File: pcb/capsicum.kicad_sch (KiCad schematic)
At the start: 45 parts, among them J1 USB4510-03-1-A_REVA, J2 Screw_Terminal_01x02, Q1 PN2222A, SW1 SW_SPDT, SW2 SW_Push_Dual, SW3 SW_SPDT, SW4 SW_Push_Dual, U1 ESP32-C3-WROOM-02, U3 AP2112K-3.3, U4 MCP73831-2-OT

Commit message: feat: associate 0603 capcitors and resistors footprints
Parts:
- C1, C2, C3, C4, C5, C6, C7, C8: footprint (none) -> Capacitor_SMD:C_0603_1608Metric
- D1, D2, D3, D4, D5, R1, R10, R11, R12, R13, R2, R3, R4, R5, R6, R7, R8, R9: footprint (none) -> Resistor_SMD:R_0603_1608Metric
- J1: footprint USB4510-03-1-A_REVA:GCT_USB4510-03-1-A_REVA -> GCT_USB_C:GCT_USB4510-03-1-A_REVA
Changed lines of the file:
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@@
       (effects (font (size 1.27 1.27)) (justify left))
     )
-    (property "Footprint" "" (at 218.44 68.58 0)
+    (property "Footprint" "Resistor_SMD:R_0603_1608Metric" (at 218.44 68.58 0)
       (effects (font (size 1.27 1.27)) hide)
     )
@@
       (effects (font (size 1.27 1.27)) (justify right))
     )
-    (property "Footprint" "" (at 218.44 62.23 0)
+    (property "Footprint" "Resistor_SMD:R_0603_1608Metric" (at 218.44 62.23 0)
       (effects (font (size 1.27 1.27)) hide)
     )
@@
       (effects (font (size 1.27 1.27)))
     )
-    (property "Footprint" "" (at 250.19 27.94 0)
+    (property "Footprint" "Resistor_SMD:R_0603_1608Metric" (at 250.19 27.94 0)
       (effects (font (size 1.27 1.27)) hide)
     )
@@
       (effects (font (size 1.27 1.27)))
     )
-    (property "Footprint" "" (at 120.65 64.77 0)
+    (property "Footprint" "Resistor_SMD:R_0603_1608Metric" (at 120.65 64.77 0)
       (effects (font (size 1.27 1.27)) hide)
     )
@@
       (effects (font (size 1.27 1.27)) (justify right))
     )
-    (property "Footprint" "" (at 196.85 73.66 0)
+    (property "Footprint" "Resistor_SMD:R_0603_1608Metric" (at 196.85 73.66 0)
       (effects (font (size 1.27 1.27)) hide)
     )
@@
       (effects (font (size 1.27 1.27)) (justify left))
     )
-    (property "Footprint" "" (at 186.69 64.77 0)
+    (property "Footprint" "Resistor_SMD:R_0603_1608Metric" (at 186.69 64.77 0)
       (effects (font (size 1.27 1.27)) hide)
     )
@@
       (effects (font (size 1.27 1.27)) (justify left))
     )
-    (property "Footprint" "" (at 20.32 48.26 0)
+    (property "Footprint" "Resistor_SMD:R_0603_1608Metric" (at 20.32 48.26 0)
       (effects (font (size 1.27 1.27)) hide)
     )
@@
       (effects (font (size 1.27 1.27)) (justify left))
     )
-    (property "Footprint" "" (at 259.08 66.04 0)
+    (property "Footprint" "Resistor_SMD:R_0603_1608Metric" (at 259.08 66.04 0)
       (effects (font (size 1.27 1.27)) hide)
     )
@@
       (effects (font (size 1.27 1.27)))
     )
-    (property "Footprint" "" (at 182.88 38.1 0)
+    (property "Footprint" "Resistor_SMD:R_0603_1608Metric" (at 182.88 38.1 0)
       (effects (font (size 1.27 1.27)) hide)
     )
@@
       (effects (font (size 1.27 1.27)) (justify left))
     )
-    (property "Footprint" "" (at 153.3652 72.39 0)
+    (property "Footprint" "Capacitor_SMD:C_0603_1608Metric" (at 153.3652 72.39 0)
       (effects (font (size 1.27 1.27)) hide)
     )
@@
       (effects (font (size 1.27 1.27)) (justify left))
     )
-    (property "Footprint" "" (at 34.29 179.07 0)
+    (property "Footprint" "Capacitor_SMD:C_0603_1608Metric" (at 34.29 179.07 0)
       (effects (font (size 1.27 1.27)) hide)
     )
@@
       (effects (font (size 1.27 1.27)) (justify left))
     )
-    (property "Footprint" "" (at 160.02 161.29 0)
+    (property "Footprint" "Resistor_SMD:R_0603_1608Metric" (at 160.02 161.29 0)
       (effects (font (size 1.27 1.27)) hide)
     )
@@
       (effects (font (size 1.27 1.27)) (justify left))
     )
-    (property "Footprint" "" (at 252.73 73.66 0)
+    (property "Footprint" "Capacitor_SMD:C_0603_1608Metric" (at 252.73 73.66 0)
       (effects (font (size 1.27 1.27)) hide)
     )
@@
       (effects (font (size 1.27 1.27)) (justify left))
     )
-    (property "Footprint" "" (at 220.98 36.83 0)
+    (property "Footprint" "Capacitor_SMD:C_0603_1608Metric" (at 220.98 36.83 0)
       (effects (font (size 1.27 1.27)) hide)
     )
@@
       (effects (font (size 1.27 1.27)))
     )
-    (property "Footprint" "USB4510-03-1-A_REVA:GCT_USB4510-03-1-A_REVA" (at 50.8 48.26 0)
+    (property "Footprint" "GCT_USB_C:GCT_USB4510-03-1-A_REVA" (at 50.8 48.26 0)
       (effects (font (size 1.27 1.27)) (justify bottom) hide)
     )
@@
       (effects (font (size 1.27 1.27)) (justify left))
     )
-    (property "Footprint" "" (at 76.2 55.88 0)
+    (property "Footprint" "Resistor_SMD:R_0603_1608Metric" (at 76.2 55.88 0)
       (effects (font (size 1.27 1.27)) hide)
     )
@@
       (effects (font (size 1.27 1.27)) (justify left))
     )
-    (property "Footprint" "" (at 143.2052 72.39 0)
+    (property "Footprint" "Capacitor_SMD:C_0603_1608Metric" (at 143.2052 72.39 0)
       (effects (font (size 1.27 1.27)) hide)
     )
@@
       (effects (font (size 1.27 1.27)))
     )
-    (property "Footprint" "" (at 105.41 62.23 0)
+    (property "Footprint" "Resistor_SMD:R_0603_1608Metric" (at 105.41 62.23 0)
       (effects (font (size 1.27 1.27)) hide)
     )
@@
       (effects (font (size 1.27 1.27)) (justify left))
     )
-    (property "Footprint" "" (at 189.23 26.67 0)
+    (property "Footprint" "Capacitor_SMD:C_0603_1608Metric" (at 189.23 26.67 0)
       (effects (font (size 1.27 1.27)) hide)
     )
@@
       (effects (font (size 1.27 1.27)) (justify left))
     )
-    (property "Footprint" "" (at 196.85 64.77 0)
+    (property "Footprint" "Resistor_SMD:R_0603_1608Metric" (at 196.85 64.77 0)
       (effects (font (size 1.27 1.27)) hide)
     )
@@
       (effects (font (size 1.27 1.27)) (justify left))
     )
-    (property "Footprint" "" (at 115.2652 76.2 0)
+    (property "Footprint" "Capacitor_SMD:C_0603_1608Metric" (at 115.2652 76.2 0)
       (effects (font (size 1.27 1.27)) hide)
     )
@@
       (effects (font (size 1.27 1.27)))
     )
-    (property "Footprint" "" (at 215.9 26.67 0)
+    (property "Footprint" "Resistor_SMD:R_0603_1608Metric" (at 215.9 26.67 0)
       (effects (font (size 1.27 1.27)) hide)
     )
@@
       (effects (font (size 1.27 1.27)) (justify left))
     )
-    (property "Footprint" "" (at 157.48 115.57 0)
+    (property "Footprint" "Resistor_SMD:R_0603_1608Metric" (at 157.48 115.57 0)
       (effects (font (size 1.27 1.27)) hide)
     )
@@
       (effects (font (size 1.27 1.27)) (justify left))
     )
-    (property "Footprint" "" (at 227.33 36.83 0)
+    (property "Footprint" "Capacitor_SMD:C_0603_1608Metric" (at 227.33 36.83 0)
       (effects (font (size 1.27 1.27)) hide)
     )
@@
       (effects (font (size 1.27 1.27)))
     )
-    (property "Footprint" "" (at 250.19 35.56 0)
+    (property "Footprint" "Resistor_SMD:R_0603_1608Metric" (at 250.19 35.56 0)
       (effects (font (size 1.27 1.27)) hide)
     )
@@
       (effects (font (size 1.27 1.27)) (justify right))
     )
-    (property "Footprint" "" (at 186.69 73.66 0)
+    (property "Footprint" "Resistor_SMD:R_0603_1608Metric" (at 186.69 73.66 0)
       (effects (font (size 1.27 1.27)) hide)
     )
@@
       (effects (font (size 1.27 1.27)))
     )
-    (property "Footprint" "" (at 205.74 22.86 0)
-      (effects (font (size 1.27 1.27)) hide)
-    )
+    (property "Footprint" "Resistor_SMD:R_0603_1608Metric" (at 205.74 22.86 0)
+      (effects (font (size 1.27 1.27)) hide)
+    )

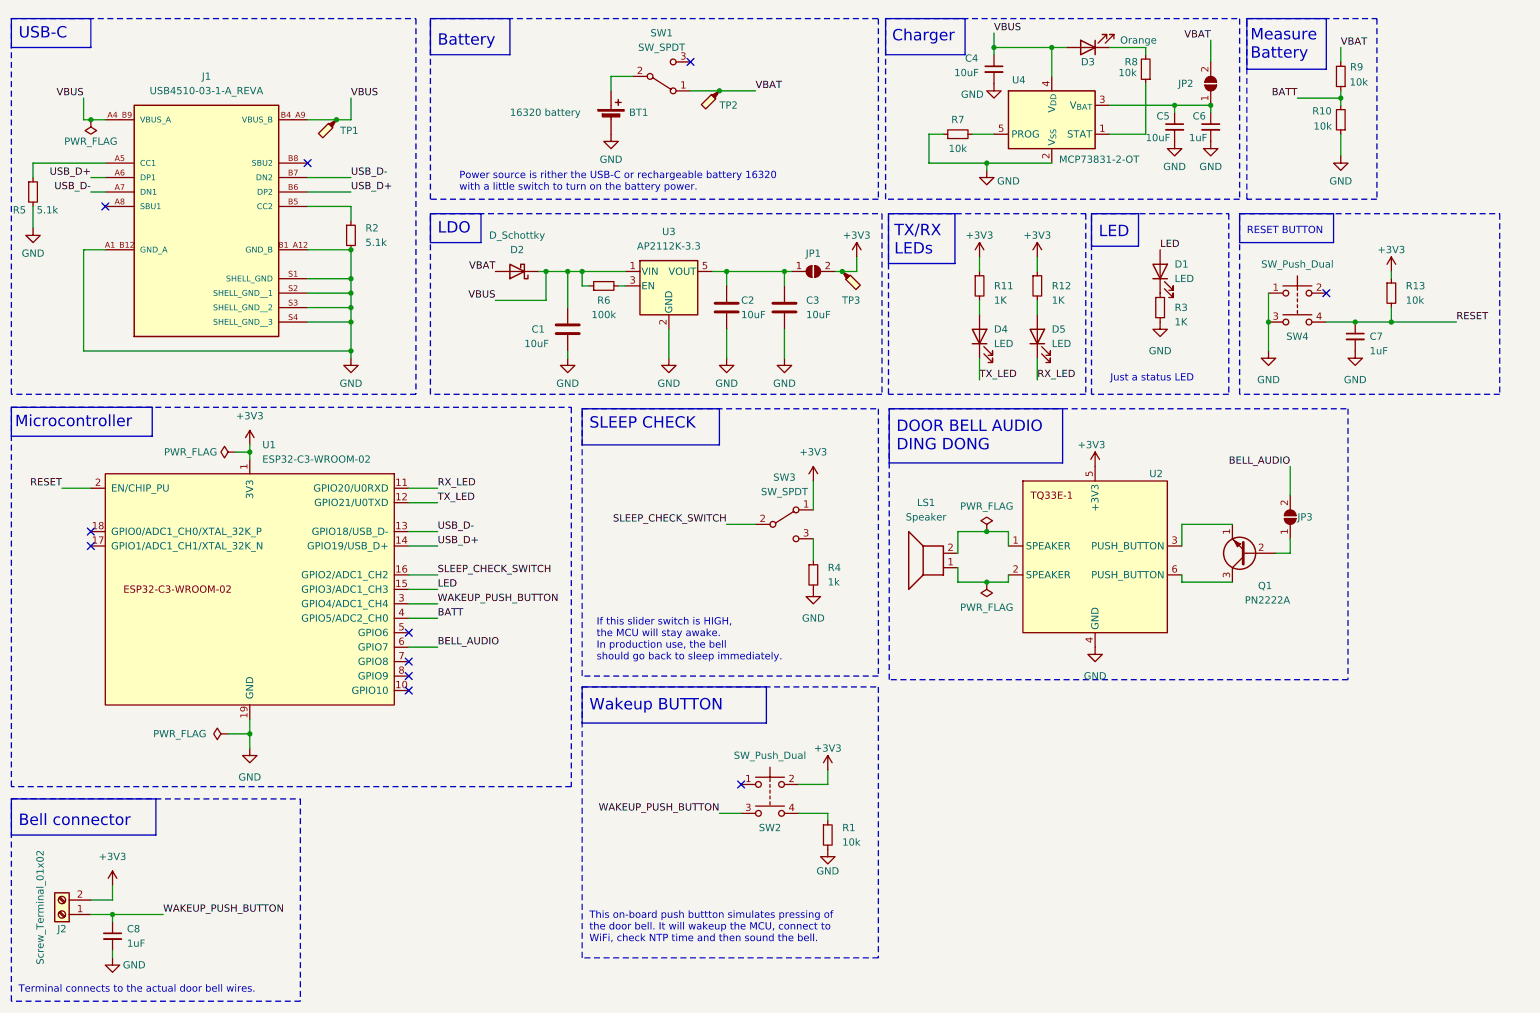
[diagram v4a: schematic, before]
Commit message: refactor: add power LEDs, combine wakeup button schematic and simplify comment
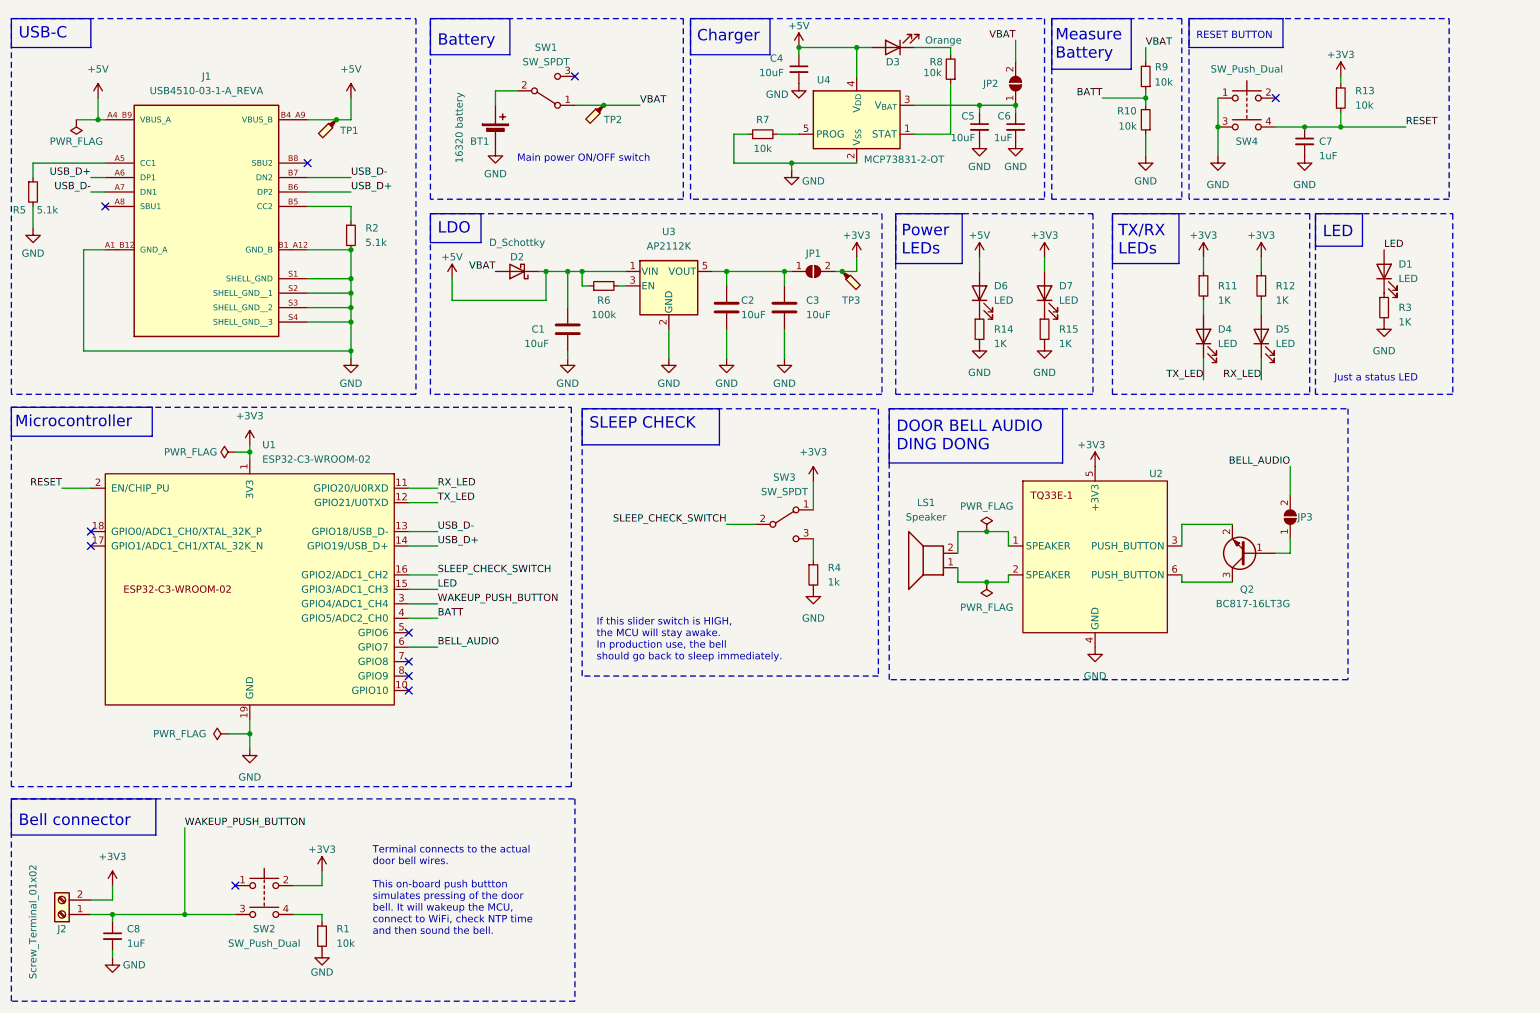
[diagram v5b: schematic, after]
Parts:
- removed Q1: PN2222A, Package_TO_SOT_THT:TO-92_Inline, symbol Transistor_BJT:PN2222A
- added D6, D7: LED, Resistor_SMD:R_0603_1608Metric, symbol Device:LED
- added Q2: BC817-16LT3G, Package_TO_SOT_SMD:SOT-23, symbol Transistor_BJT:BC817
- added R14, R15: 1K, Resistor_SMD:R_0603_1608Metric, symbol Device:R_Small
- C1, C2, C3, C4, C5: Link (none) -> https://www.pcbway.com/components/detail/CC0603KRX5R6BB106/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; MPN (none) -> CC0603KRX5R6BB106; Vendor (none) -> PCBWay
- C6, C7, C8: Link (none) -> https://www.pcbway.com/components/detail/06033D105MAT2A/217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; MPN (none) -> 06033D105MAT2A; Vendor (none) -> PCBWay
- U3: value AP2112K-3.3 -> AP2112K; Link (none) -> https://www.pcbway.com/components/detail/AP2112K33TRG1/1123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; MPN (none) -> AP2112K-3.3TRG1
- U4: MPN (none) -> MCP73831-2-OT
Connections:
- net +3V3: now also D7.2 (A)
- net GND: now also R14.2, R15.2
- net at U2.3 (PUSH_BUTTON): now also Q2.2 (E)
- net at JP3.1 (A): now also Q2.1 (B)
- net at U2.6 (PUSH_BUTTON): now also Q2.3 (C)
- net VBUS renamed +5V
- net +5V: now also D6.2 (A)
- new net: D6.1 (K), R14.1
- new net: D7.1 (K), R15.1
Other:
- note added: "Main power ON/OFF switch"
- note added: "Power LEDs"
- note added: "Terminal connects to the actual door bell wires. This on-board push buttton simulates pressing of the door bell. It will wakeup the MCU, connect to WiFi, check NTP time and then sound the bell."
- note removed: "Power source is rither the USB-C or rechargeable battery 16320 with a little switch to turn on the battery power."
- note removed: "Terminal connects to the actual door bell wires."
- note removed: "This on-board push buttton simulates pressing of the door bell. It will wakeup the MCU, connect to WiFi, check NTP time and then sound the bell."
- note removed: "Wakeup BUTTON"
- moved on the sheet: BT1, C4, C5, C6, C7, D1, D3, D4, D5, JP2, R1, R10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

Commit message: refactor: add battery measurement circuit that saves power draw
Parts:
- added C9: 0.1uF, symbol Device:C_Small
- added Q1: BSS83P, Package_TO_SOT_SMD:SOT-23, symbol Transistor_FET:BSS83P
- added R16: 1M, Resistor_SMD:R_0603_1608Metric, symbol Device:R_Small
- R10: value 10k -> 100k
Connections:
- net +3V3: now also D4.2 (A), D5.2 (A); no longer R11.1, R12.1
- net RX_LED: now also R12.2; no longer D5.1 (K)
- net TX_LED: now also R11.2; no longer D4.1 (K)
- net VBAT: now also Q1.2 (S), R16.2; no longer R9.2
- net BATT_EN: now reaches U1.5 (GPIO6)
- net BATT_EN: now also C9.2
- new net: C9.1, Q1.1 (G), R16.1
- new net: Q1.3 (D), R9.2
- new net: D5.1 (K), R12.1
- new net: D4.1 (K), R11.1
- no-connect marks 11 -> 10
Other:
- note added: "Measure BATT"
- note removed: "Measure Battery"
- moved on the sheet: C7, D1, D4, D5, R10, R11, R12, R13, R3, R9, SW4

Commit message: feat: associate package to LDO and charger
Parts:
- U3: Package (none) -> SOT-23-5 or SOT-753 or SOT-25
- U4: Link (none) -> https://www.pcbway.com/components/detail/MCP73831T2ACIOT/28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; MPN MCP73831-2-OT -> MCP73831T-2ACI/OT; Package (none) -> SOT-23-5; Vendor (none) -> PCBWay
